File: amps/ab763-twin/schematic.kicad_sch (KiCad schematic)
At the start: 130 parts, among them T1 125P34A · 340-0-340 V, T2 125C1A, T3 125A29A, T4 125A20B

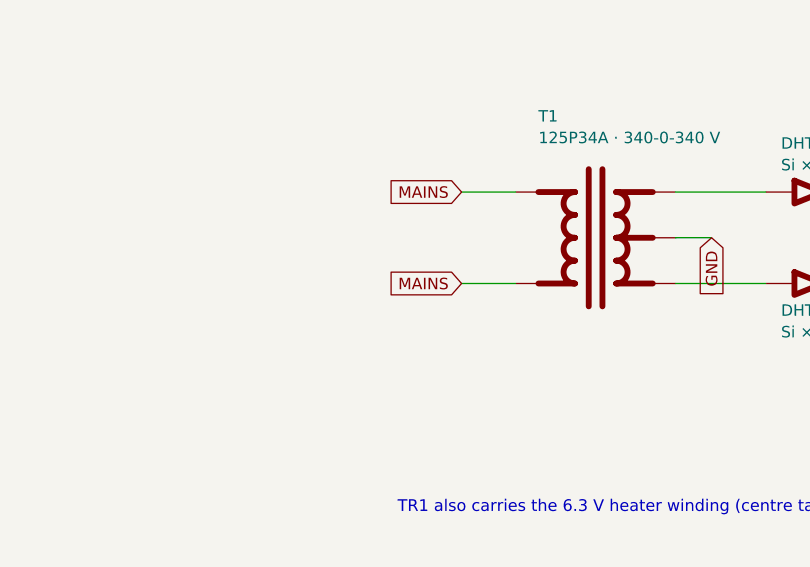
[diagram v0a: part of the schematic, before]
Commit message: Fix: the 6G5's rectifier was connected to nothing; 17 sheets shorted the mains by naming both leads alike
6G5 power supply. The sheet drew four diodes as a "silicon bridge" whose
HT_A/HT_B labels stopped 6 mm short of their wires. D1/D2's anodes sat on
the tremolo's cathode node (a tremolo wire's end touched the old diode
stub), D3/D4 ran from ground to the reservoir, and TR1's centre tap floated
under an open-pin waiver whose stated reason was the bridge itself.
A-FJ (Schematic Heaven 2153x1437, read enlarged): each HT end of TR1 runs
through a leg of three silicon diodes, every + (cathode) toward the +460 V
reservoir; the centre tap is grounded; TR1's second secondary terminal is a
bias tap feeding the 6G4's network part for part: rectifier, 8-150, 10K,
then 8-150 and a 56K bleeder at the -55 V line. Redrawn as the drawing
shows: D1-D6, TR1 with its tap pin, the centre tap to ground, the bias
network (CBIAS 25 uF -> 8 uF; RBIAS2, CBIAS2, RBIAS1 added), the waiver
deleted, and the notes, meta, netlist header and parts list no longer say
bridge. Not yet carried: the drawing's second 20-600 at the reservoir and
the standby switch (this sheet omits chassis switches by its own note);
and the tremolo ladder still runs through the transformer's corner of the
sheet, a layout clash rather than a connection, queued for its own redraw.

Mains. Two global labels with one name are one net. 16 of 24 power
transformers on the sheets carried a label named MAINS on both primary
leads, so the winding's two pins were one net: 5E4-A, 5E5-A, 5F4, 5G9,
6161, 6G2, 6G3, 6G4, AA1164, AA764, AA764-Vibro, AA964, AB763, AB763
Super, AB763 Twin, GA-40. The 6G5's loop ran from one MAINS label through
switch, fuse and winding back to the same name. No gate models the primary,
so a copy-pasted idiom did this. The second lead is now MAINS N, the AC15's
idiom; the AA1164's and AA964's second AC row, drawn under the first row's
name, is the neutral. The death and across-the-line caps stay on the le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
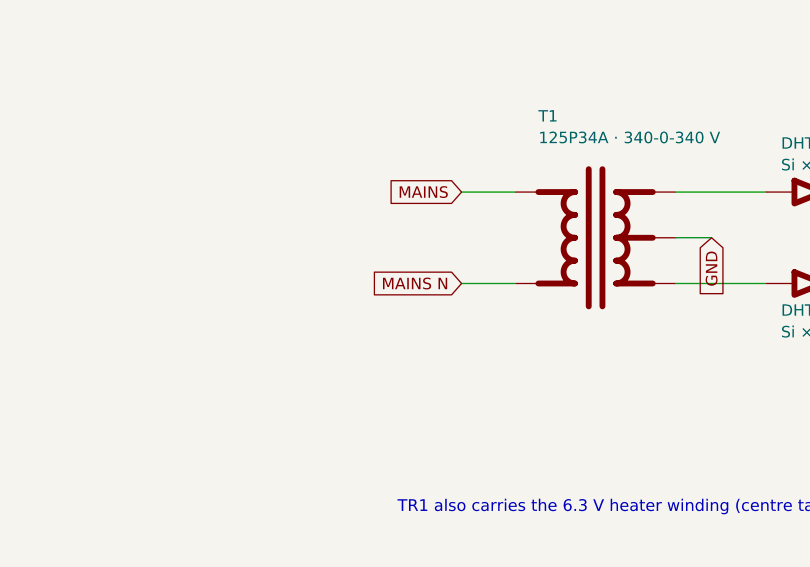
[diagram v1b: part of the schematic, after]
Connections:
- net MAINS: no longer T1.2 (PRI_2)
- new net MAINS N: T1.2 (PRI_2)
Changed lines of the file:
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@@
   (wire (pts (xy 266.719 330.969) (xy 260.719 330.969))
     (stroke (width 0) (type default)))
-  (global_label "MAINS" (shape input) (at 260.719 330.969 180)
+  (global_label "MAINS N" (shape input) (at 260.719 330.969 180)
     (effects (font (size 1.27 1.27)) (justify right)))
   (wire (pts (xy 284.499 325.889) (xy 288.499 325.889))

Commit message: Fix: AB763 Twin mixer, photocell and tremolo ladder drawn as the C-FD sheet draws them
- The photocell sat on the mix driver's grid. On the drawing (read at
  6138 x 4384) the 50K-RA Intensity control hangs from the mix driver's
  OUTPUT, between CCD1 .1 and RMIXV 220K, and the photocell runs from its
  wiper to ground. VRINT now hangs there and reaches the photocell by label.
- The 470K reverb return (RMR) and the 220K leak (RTOG4) sat on the dry side
  of the 3.3M || 10PF. The drawing lands both on V4A's grid side. The dry node
  carries only CCV2 .02, the 500PF send and RGD1/CBD1. Its new DRY label also
  replaces a MIXG label that stopped 4 mm short of its wire, so the old dry
  path never reached the grid.
- Tremolo ladder: the lamp driver's grid was on the Speed node, and N1's 1M
  landed on the grid. The drawing: plate -> .02 -> Speed node -> .01 -> N1
  (lamp-driver grid; 1M to J) -> .01 -> grid (1M to J), and J -> 2.2M -> the
  bias supply's filter node, which was drawn as ground. The filter node now
  has a label.
- netlist.cir: the mix driver's DC grid return is now RTOG4 220k to ground. It
  was RGD1 3.3M to ground, which on the drawing reaches only a DC-blocked
  node. No gated value moves. The sch_map series_bridge that folded RTOG4
  into node 0 is retired.
- bom.yaml and notes.md: the mixer, Intensity and tremolo roles and prose
  now follow the drawing.
- The board (held for repair) still wires RGD1 as a grid leak to ground.
  verify_layout_nets reports RTOG4 missing from the board until
  net_map.netlist_unplaced declares it, and sheet-vs-board adds MISPLACED RGD1.

Co-Authored-By: Claude Opus 5 (1M context) <noreply@anthropic.com>
Claude-Session: https://claude.ai/code/session_01KBMfdh37HmCL2iWcBiL5J1
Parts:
- removed CBD1: 10p, symbol cx:C
- removed DHTB: Si ×3, symbol cx:DIODE_SS
- removed RD1: 1k 1W, symbol cx:R
- removed RD2: 4.7k 1W, symbol cx:R
- removed RLPA: 82k 5%, symbol cx:R
- removed RSC1, RSC2, RSC3, RSC4: 470 1W, symbol cx:R
- removed RTOG3: 2.2M, symbol cx:R
- removed V5A: 12AX7, symbol cx:TRIODE
- removed VRBAL: 10k-L bal, symbol cx:POT
- removed VRINT: 50k-RA int, symbol cx:POT
- added C12, C13: 20u 525V, symbol cx:C
- added DHTA: Si ×3, symbol cx:DIODE_SS
- added RB2: 27k, symbol cx:R
- added RKE: 820, symbol cx:R
- added RKTO2: 100k, symbol cx:R
- added RST1, RST2, RST3, RST4: 1.5k, symbol cx:R
- added RTOG4: 220k, symbol cx:R
- added V6B: 12AT7, symbol cx:TRIODE
- added VRSPD: 3M-RA speed, symbol cx:POT
- CBD1: renamed from RGD1; value 3.3M -> 10p; symbol cx:R -> cx:C
- CKTO1: renamed from VRSPD; value 3M-RA speed -> 25u; symbol cx:POT -> cx:C
- RD1: renamed from C12; value 20u 525V -> 1k 1W; symbol cx:C -> cx:R
- RD2: renamed from C13; value 20u 525V -> 4.7k 1W; symbol cx:C -> cx:R
- RGD1: renamed from RTOG4; value 220k -> 3.3M
- RLPA: renamed from V6B; value 12AT7 -> 82k 5%; symbol cx:TRIODE -> cx:R
- RSC1: renamed from V7; value 6L6GC -> 470 1W; symbol cx:PENTODE -> cx:R
- RSC2: renamed from V8; value 6L6GC -> 470 1W; symbol cx:PENTODE -> cx:R
- RSC3: renamed from V9; value 6L6GC -> 470 1W; symbol cx:PENTODE -> cx:R
- RSC4: renamed from V10; value 6L6GC -> 470 1W; symbol cx:PENTODE -> cx:R
- RTOG3: renamed from RKTO2; value 100k -> 2.2M
- V10: renamed from RST4; value 1.5k -> 6L6GC; symbol cx:R -> cx:PENTODE
- V5A: renamed from CKTO1; value 25u -> 12AX7; symbol cx:C -> cx:TRIODE
- V7: renamed from RST1; value 1.5k -> 6L6GC; symbol cx:R -> cx:PENTODE
- V8: renamed from RST2; value 1.5k -> 6L6GC; symbol cx:R -> cx:PENTODE
- V9: renamed from RST3; value 1.5k -> 6L6GC; symbol cx:R -> cx:PENTODE
- VRBAL: renamed from RB2; value 27k -> 10k-L bal; symbol cx:R -> cx:POT
- VRINT: renamed from RKE; value 820 -> 50k-RA int; symbol cx:R -> cx:POT
- renumbered DHTA to DHTB
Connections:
- net -52V: now also VRBAL.2 (W)
- net B+1: now also DHTA.2 (K)
- net B+2: now also RLAMP.2, RSC1.2, RSC2.2, RSC3.2, RSC4.2, RTO10.1, C12.1; no longer RLAMP.1, RTO10.2
- net B+3: now also RD1.2, RLPA.1, C13.1
- net B+4: now also RD2.2
- net GND: now also CKTO1.2, OPTO.4 (P2), V10.4 (K), V7.4 (K), V8.4 (K), V9.4 (K), VRINT.3, C12.2, C13.2, RB2.2, RKE.2, RKTO2.2, RTOG4.2; no longer RD1.2, RD2.2, RGD1.2, RSC1.4 (K), RSC2.4 (K), RSC3.4 (K), RSC4.4 (K), RTOG3.2, V5A.2, VRBAL.2, VRINT.2
- net at V7.1 (P), V8.1 (P): now also T3.1 (PRI_A); no longer C1.2, RGL1.2
- net at V7.2 (G1): now also RST1.2; no longer RSC1.2 (G1)
- net at CTO1.1, RTOG1.2: now also CTO2.1, V5B.2 (G); no longer CTO2.2
- net at DHTB.1 (A): now also T1.5 (HT_B); no longer T1.3 (HT_A)
- net at V5A.1 (P): now also CTO3.1, RTO1.2; no longer RKTO1.1
- net at CKE.1, V4A.3 (K), V4B.3 (K): now also RKE.1; no longer VRINT.1
- net at OPTO.2 (L2): now also RLAMP.1; no longer RLAMP.2
- net at CKTO2.1, V5B.3 (K): now also RKTO2.1; no longer RTOG3.1
- net at CBD1.2, V4A.2 (G): now also RGD1.2, RMR.2, RTOG4.1
- net at CCD1.2, RMIXV.1: now also VRINT.1
- net BIAS FILTER: now reaches CB1.1, DBIAS.1 (A)
- net BIAS FILTER: now also RTOG3.2, VRBAL.1
- net at C2.2, RGL2.1: now also RST3.1, RST4.1; no longer V10.1, V9.1
- net at V9.2 (G1): now also RST3.2; no longer RSC3.2 (G1)
- net at OPTO.1 (L1), V5B.1 (P): now also RTO10.2; no longer RTO10.1
- net DRY: now reaches CBD1.1, RGD1.1
- net DRY: now also CCV2.2, CRS.2
- net at C2.1, RLPB.2: now also V6B.1 (P); no longer RLPA.1 (P)
- net at CPIB.2, RGPB.2: now also V6B.2 (G); no longer RLPA.2 (G)
- net at RTAIL.2, V6A.3 (K): now also V6B.3 (K); no longer RLPA.3 (K)
- net at RTOG2.1: now also RTOG1.1, RTOG3.1
- net at V10.2 (G1): now also RST4.2; no longer RSC4.2 (G1)
- net at RTOSP.1: now also VRSPD.3; no longer CKTO1.3
- net at V8.2 (G1): now also RST2.2; no longer RSC2.2 (G1)
- net at C1.1, V6A.1 (P): now also RLPA.2
- removed net MIXG: CCV2.2, CRS.2, OPTO.3 (P1), RMR.2
- new net: RSC1.1, V7.3 (G2)
- new net: CTO1.2, CTO3.2, VRSPD.2 (W)
- new net: CKTO1.1, RKTO1.1, V5A.3 (K)
- new net: T3.3 (PRI_B), V10.1 (P), V9.1 (P)
- new net: RSC3.1, V9.3 (G2)
- new net: C1.2, RGL1.2, RST1.1, RST2.1
- new net: CTO2.2, RTOG2.2, V5A.2 (G)
- new net: RSC4.1, V10.3 (G2)
- new net: RB2.1, VRBAL.3
- new net: RSC2.1, V8.3 (G2)
- new net: DHTA.1 (A), T1.3 (HT_A)
- new net PHOTOCELL: OPTO.3 (P1), VRINT.2 (W)
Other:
- note added: "Dry node → 3.3 MΩ (10 pF across it) → mix-driver grid, where the 470 kΩ reverb return and the 220 kΩ grid leak land"
- note added: "The vibrato footswitch grounds the junction of the two 1 MΩ ladder resistors and the 2.2 MΩ, and stops the oscillator"
- note added: "Tremolo — oscillator V5A and neon-lamp driver V5B; neither half has a static DC operating point, so both are excluded from the netlist (see the circuit story)"
- note removed: "Mix node: the vibrato channel's dry signal, the reverb return through the 470 kΩ, and the tremolo photocell all land here; the 220 kΩ returns it to ground"
- note removed: "The vibrato footswitch grounds this bus and stops the oscillator"
- note removed: "Tremolo oscillator (V5) + optocoupler — dynamic; neither half has a static DC operating point, so both are excluded from the netlist (see the circuit story)"
- moved on the sheet: DHTB, RGD1, RTOG3

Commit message: Fix: AB763 Twin reverb-recovery grid leak, tremolo sections and the dry-node corner, as the C-FD drawings show them
- RGR1 220K is the recovery grid's leak to ground, and the tank return lands
  straight on the grid (schematic read at 6138 x 4384, crop t-recov). The
  sheet drew the 220K in series from the tank return, and an sch_map anchor
  folded that lead into ground to match the netlist. The anchor is retired.
- V5: the layout page (read at 2157 x 1397) leads the oscillator's +300 V
  plate to pin 1 and its +2.0 V cathode to pin 3, and the lamp driver's
  +380 V plate to pin 6. The sheet lettered the halves the other way round:
  V5A is now datasheet unit 2 and V5B unit 1, as the board already wires them.
- netlist.cir: the dry node GDRY is modelled. RGD1 3.3meg and CBD1 10p run
  from it to the mix grid, CCV2 0.02u from the V2B plate, and CRS 500p to
  the reverb-driver grids. The netlist's own rule models a DC-open part when
  both leads land on named DC nodes, and it makes this corner's board
  placement machine-checked. The board places all four there, and the
  op-point is unmoved.

Co-Authored-By: Claude Opus 5 (1M context) <noreply@anthropic.com>
Claude-Session: https://claude.ai/code/session_01KBMfdh37HmCL2iWcBiL5J1
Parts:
- removed C12, C13: 20u 525V, symbol cx:C
- removed DHTA: Si ×3, symbol cx:DIODE_SS
- removed RKTO1: 2.7k, symbol cx:R
- removed RKTO2: 100k, symbol cx:R
- removed RST1, RST2, RST3, RST4: 1.5k, symbol cx:R
- removed V5B: 12AX7, symbol cx:TRIODE
- removed V6B: 12AT7, symbol cx:TRIODE
- removed VRBAL: 10k-L bal, symbol cx:POT
- added CKTO1, CKTO2: 25u, symbol cx:C
- added DHTB: Si ×3, symbol cx:DIODE_SS
- added RB2: 27k, symbol cx:R
- added RD1: 1k 1W, symbol cx:R
- added RD2: 4.7k 1W, symbol cx:R
- added RLPA: 82k 5%, symbol cx:R
- added RSC1, RSC2, RSC3, RSC4: 470 1W, symbol cx:R
- added RTO1: 220k, symbol cx:R
- C12: renamed from RD1; value 1k 1W -> 20u 525V; symbol cx:R -> cx:C
- C13: renamed from RD2; value 4.7k 1W -> 20u 525V; symbol cx:R -> cx:C
- RKTO1: renamed from CKTO1; value 25u -> 2.7k; symbol cx:C -> cx:R
- RKTO2: renamed from CKTO2; value 25u -> 100k; symbol cx:C -> cx:R
- RST1: renamed from V7; value 6L6GC -> 1.5k; symbol cx:PENTODE -> cx:R
- RST2: renamed from V8; value 6L6GC -> 1.5k; symbol cx:PENTODE -> cx:R
- RST3: renamed from V9; value 6L6GC -> 1.5k; symbol cx:PENTODE -> cx:R
- RST4: renamed from V10; value 6L6GC -> 1.5k; symbol cx:PENTODE -> cx:R
- V10: renamed from RSC4; value 470 1W -> 6L6GC; symbol cx:R -> cx:PENTODE
- V5A: Basing_unit (none) -> 2
- V5B: renamed from RTO1; value 220k -> 12AX7; symbol cx:R -> cx:TRIODE; Basing_unit (none) -> 1
- V6B: renamed from RLPA; value 82k 5% -> 12AT7; symbol cx:R -> cx:TRIODE
- V7: renamed from RSC1; value 470 1W -> 6L6GC; symbol cx:R -> cx:PENTODE
- V8: renamed from RSC2; value 470 1W -> 6L6GC; symbol cx:R -> cx:PENTODE
- V9: renamed from RSC3; value 470 1W -> 6L6GC; symbol cx:R -> cx:PENTODE
- VRBAL: renamed from RB2; value 27k -> 10k-L bal; symbol cx:R -> cx:POT
- renumbered DHTB to DHTA
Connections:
- net -52V: now also VRBAL.2 (W)
- net B+1: now also DHTB.2 (K)
- net B+2: now also RD1.1, RSC1.2, RSC2.2, RSC3.2, RSC4.2, RTO1.1; no longer V10.2, V5B.1, V7.2, V8.2, V9.2
- net B+3: now also RD1.2, RD2.1, RLPA.1; no longer C12.2, V6B.1
- net B+4: now also RD2.2; no longer C13.2
- net BIAS FILTER: now also VRBAL.1
- net GND: now also C12.2, C13.2, RGR1.2, V10.4 (K), V7.4 (K), V8.4 (K), V9.4 (K), CKTO1.2, CKTO2.2, RB2.2; no longer RST1.4 (K), RST2.4 (K), RST3.4 (K), RST4.4 (K), VRBAL.2
- net TANK RET: now also V4B.2 (G)
- net at RST1.1, RST2.1: now also C1.2, RGL1.2; no longer T3.1 (PRI_A)
- net at RST1.2: now also V7.2 (G1)
- net at V7.1 (P): now also T3.1 (PRI_A), V8.1 (P); no longer RST1.3 (G2)
- net at DHTA.1 (A): now also T1.3 (HT_A); no longer T1.5 (HT_B)
- net at CTO3.1, V5A.1 (P): now also RTO1.2; no longer V5B.2
- net at RKTO1.1, V5A.3 (K): now also CKTO1.1
- net at C2.1, RLPB.2: now also V6B.1 (P)
- net at C2.2, RGL2.1: now also RST3.1, RST4.1
- net at OPTO.1 (L1), RTO10.2: now also V5B.1 (P)
- net at RKTO2.1: now also V5B.3 (K), CKTO2.1
- net at RST3.2: now also V9.2 (G1)
- net at V9.1 (P): now also T3.3 (PRI_B), V10.1 (P); no longer RST3.3 (G2)
- net at C1.1, V6A.1 (P): now also RLPA.2; no longer V6B.2
- net at CTO1.1, CTO2.1, RTOG1.2: now also V5B.2 (G)
- net at RTAIL.2, V6A.3 (K): now also V6B.3 (K)
- net at CPIB.2, RGPB.2: now also V6B.2 (G)
- net at RST4.2: now also V10.2 (G1)
- net at RST2.2: now also V8.2 (G1)
- new net: DHTB.1 (A), T1.5 (HT_B)
- new net: RSC2.1, V8.3 (G2)
- new net: RSC4.1, V10.3 (G2)
- new net: RSC1.1, V7.3 (G2)
- new net: RB2.1, VRBAL.3
- new net: RSC3.1, V9.3 (G2)
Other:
- moved on the sheet: DHTA
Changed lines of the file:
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@@
   (global_label "TANK RET" (shape input) (at 157.609 165.889 180)
     (effects (font (size 1.27 1.27)) (justify right)))
-  (symbol (lib_id "cx:R") (at 169.609 165.889 90) (unit 1)
-    (in_bom yes) (on_board yes)
-    (property "Reference" "RGR1" (at 166.409 159.889 270) (effects (font (size 1.27 1.27)) (justify left)))
-    (property "Value" "220k" (at 166.409 162.289 270) (effects (font (size 1.27 1.27)) (justify left))))
-  (wire (pts (xy 157.609 165.889) (xy 165.799 165.889))
-    (stroke (width 0) (type default)))
-  (wire (pts (xy 173.419 165.889) (xy 179.609 165.889))
-    (stroke (width 0) (type default)))
+  (wire (pts (xy 157.609 165.889) (xy 165.609 165.889))
+    (stroke (width 0) (type default)))
+  (wire (pts (xy 165.609 165.889) (xy 179.609 165.889))
+    (stroke (width 0) (type default)))
+  (junction (at 165.609 165.889) (diameter 1.7) (color 0 0 0 0))
+  (symbol (lib_id "cx:R") (at 165.609 169.699 0) (unit 1)
+    (in_bom yes) (on_board yes)
+    (property "Reference" "RGR1" (at 167.809 166.499 0) (effects (font (size 1.27 1.27)) (justify left)))
+    (property "Value" "220k" (at 167.809 168.899 0) (effects (font (size 1.27 1.27)) (justify left))))
+  (global_label "GND" (shape input) (at 165.609 173.509 270)
+    (effects (font (size 1.27 1.27)) (justify right)))
   (wire (pts (xy 179.609 165.889) (xy 179.609 171.889))
     (stroke (width 0) (type default)))
@@
     (in_bom yes) (on_board yes)
     (property "Reference" "V5A" (at 83.6088 275.489 0) (effects (font (size 1.27 1.27)) (justify left)))
-    (property "Value" "12AX7" (at 83.6088 277.889 0) (effects (font (size 1.27 1.27)) (justify left))))
+    (property "Value" "12AX7" (at 83.6088 277.889 0) (effects (font (size 1.27 1.27)) (justify left)))
+    (property "Basing_unit" "2" (at 83.6088 280.289 0) (effects (font (size 1.27 1.27)) hide)))
   (symbol (lib_id "cx:TRIODE") (at 143.609 281.889 0) (unit 1)
     (in_bom yes) (on_board yes)
     (property "Reference" "V5B" (at 149.609 275.489 0) (effects (font (size 1.27 1.27)) (justify left)))
-    (property "Value" "12AX7" (at 149.609 277.889 0) (effects (font (size 1.27 1.27)) (justify left))))
+    (property "Value" "12AX7" (at 149.609 277.889 0) (effects (font (size 1.27 1.27)) (justify left)))
+    (property "Basing_unit" "1" (at 149.609 280.289 0) (effects (font (size 1.27 1.27)) hide)))
   (wire (pts (xy 77.6088 274.269) (xy 77.6088 270.789))
     (stroke (width 0) (type default)))
@@
   (text "8" (at 252.459 200.239 0)
     (effects (font (size 1.1 1.1)) (justify left)))
-  (text "6" (at 78.4588 275.539 0)
-    (effects (font (size 1.1 1.1)) (justify left)))
-  (text "7" (at 70.6616 280.489 0)
-    (effects (font (size 1.1 1.1)) (justify left)))
-  (text "8" (at 78.4588 288.239 0)
-    (effects (font (size 1.1 1.1)) (justify left)))
-  (text "1" (at 144.459 275.539 0)
-    (effects (font (size 1.1 1.1)) (justify left)))
-  (text "2" (at 136.662 280.489 0)
-    (effects (font (size 1.1 1.1)) (justify left)))
-  (text "3" (at 144.459 288.239 0)
+  (text "1" (at 78.4588 275.539 0)
+    (effects (font (size 1.1 1.1)) (justify left)))
+  (text "2" (at 70.6616 280.489 0)
+    (effects (font (size 1.1 1.1)) (justify left)))
+  (text "3" (at 78.4588 288.239 0)
+    (effects (font (size 1.1 1.1)) (justify left)))
+  (text "6" (at 144.459 275.539 0)
+    (effects (font (size 1.1 1.1)) (justify left)))
+  (text "7" (at 136.662 280.489 0)
+    (effects (font (size 1.1 1.1)) (justify left)))
+  (text "8" (at 144.459 288.239 0)
     (effects (font (size 1.1 1.1)) (justify left)))
   (text "6" (at 344.459 89.539 0)
